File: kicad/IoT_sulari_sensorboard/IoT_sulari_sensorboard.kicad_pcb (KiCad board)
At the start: 2 copper layers, 12.9 x 17.5 mm, 8 parts, among them J1 20021121-00010C4LF, U1 SHT40-AD1B-R3, U2 TMP117MAIDRVT

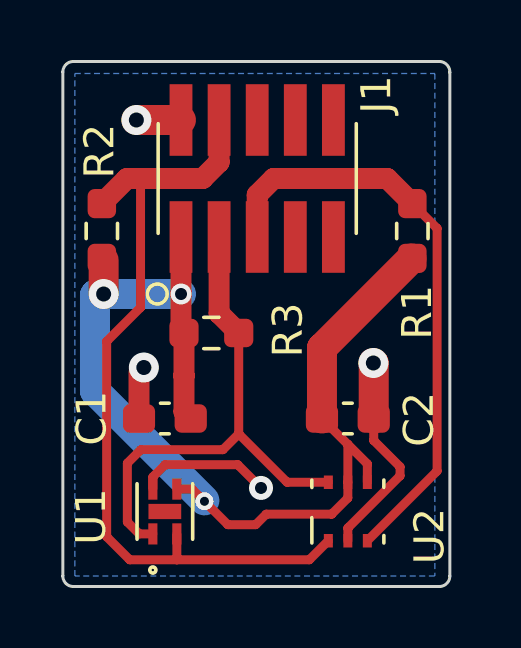
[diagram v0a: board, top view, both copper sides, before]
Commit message: Edited copper fill zones, final touches
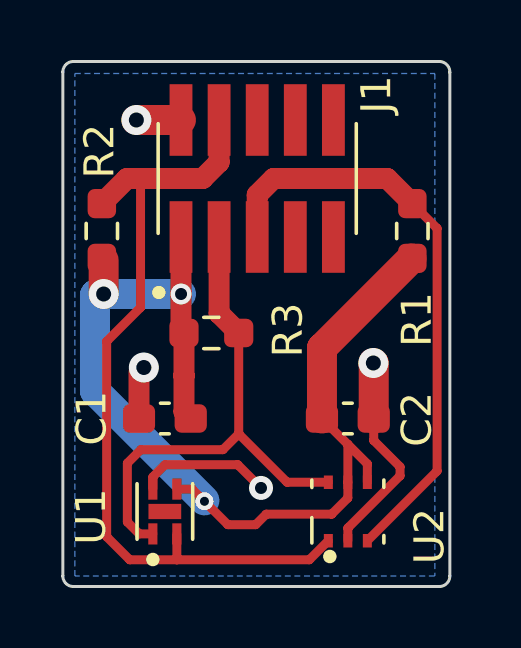
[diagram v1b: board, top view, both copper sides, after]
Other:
- outline, holes or cut-outs redrawn
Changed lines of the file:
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@@
     (property "ki_keywords" "R res resistor")
     (attr smd)
-    (fp_text reference "R1" (at -2.71 0.16 90) (layer "F.SilkS")
+    (fp_text reference "R1" (at -2.95 0.15 90) (layer "F.SilkS")
         (effects (font (size 1 1) (thickness 0.153)))
     )
@@
     (property "ki_keywords" "cap capacitor")
     (attr smd)
-    (fp_text reference "C2" (at 2.37 0.03 90) (layer "F.SilkS")
+    (fp_text reference "C2" (at 2.3 0.03 90) (layer "F.SilkS")
         (effects (font (size 1 1) (thickness 0.153)))
     )
@@
     (fp_line (start 0.9271 -0.9271) (end -0.9271 -0.9271)
       (stroke (width 0.12) (type solid)) (layer "F.SilkS"))
-    (fp_circle (center -1.950899 -0.4) (end -1.849299 -0.4)
-      (stroke (width 0.12) (type solid)) (fill none) (layer "F.SilkS"))
     (fp_line (start -3.4139 -0.654) (end -3.1599 -0.654)
       (stroke (width 0.1) (type solid)) (layer "Cmts.User"))
@@
     (fp_line (start 3.302 1.8288) (end 3.302 -1.8288)
       (stroke (width 0.12) (type solid)) (layer "F.SilkS"))
-    (fp_circle (center -3.331 3.85) (end -3.001 3.85)
-      (stroke (width 0.12) (type solid)) (fill none) (layer "F.SilkS"))
     (fp_line (start -13.462 -1.9558) (end -13.208 -1.9558)
       (stroke (width 0.1) (type solid)) (layer "Cmts.User"))
@@
       (net 10 "unconnected-(J1-Pad10)") (pinfunction "10") (pintype "no_connect"))
   )
+  (gr_circle (center 134.8 89.8) (end 134.95 89.8)
+    (stroke (width 0.15) (type solid)) (fill solid) (layer "F.SilkS"))
+  (gr_circle (center 134.6 98.7) (end 134.75 98.7)
+    (stroke (width 0.15) (type solid)) (fill solid) (layer "F.SilkS"))
+  (gr_circle (center 140.5 98.6) (end 140.65 98.6)
+    (stroke (width 0.15) (type solid)) (fill solid) (layer "F.SilkS"))
   (gr_line (start 137.5 82.1) (end 142.7 82.1)
     (stroke (width 0.1) (type default)) (layer "Edge.Cuts"))
@@
   (gr_arc (start 131.599858 82.449999) (mid 131.705973 82.198901) (end 131.96 82.1)
     (stroke (width 0.1) (type default)) (layer "Edge.Cuts"))
-  (gr_line (start 137.5 82.1) (end 131.95 82.1)
+  (gr_line (start 137.5 82.1) (end 131.96 82.1)
     (stroke (width 0.1) (type default)) (layer "Edge.Cuts"))
   (gr_line (start 144.5 82.464152) (end 144.500142 99.25)
@@
   (gr_arc (start 131.949999 99.600142) (mid 131.698901 99.494027) (end 131.6 99.24)
     (stroke (width 0.1) (type default)) (layer "Edge.Cuts"))
-  (gr_line (start 142.7 82.1) (end 144.16 82.1)
+  (gr_line (start 142.7 82.1) (end 144.126713 82.100001)
     (stroke (width 0.1) (type default)) (layer "Edge.Cuts"))
   (gr_line (start 131.6 99.24) (end 131.599858 82.449999)

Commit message: Add sensorboard manufacturing files
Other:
- rule pad_to_mask_clearance: 0.05 -> 0
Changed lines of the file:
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@@
       (dielectric_constraints no)
     )
-    (pad_to_mask_clearance 0.05)
+    (pad_to_mask_clearance 0)
     (pcbplotparams
       (layerselection 0x00010fc_ffffffff)
       (plot_on_all_layers_selection 0x0000000_00000000)
       (disableapertmacros false)
-      (usegerberextensions false)
-      (usegerberattributes true)
-      (usegerberadvancedattributes true)
-      (creategerberjobfile true)
+      (usegerberextensions true)
+      (usegerberattributes false)
+      (usegerberadvancedattributes false)
+      (creategerberjobfile false)
       (dashed_line_dash_ratio 12.000000)
       (dashed_line_gap_ratio 3.000000)
@@
       (psa4output false)
       (plotreference true)
-      (plotvalue true)
+      (plotvalue false)
       (plotinvisibletext false)
       (sketchpadsonfab false)
-      (subtractmaskfromsilk false)
+      (subtractmaskfromsilk true)
       (outputformat 1)
       (mirror false)
-      (drillshape 1)
+      (drillshape 0)
       (scaleselection 1)
       (outputdirectory "")
